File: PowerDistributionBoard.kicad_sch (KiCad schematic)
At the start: 0 parts

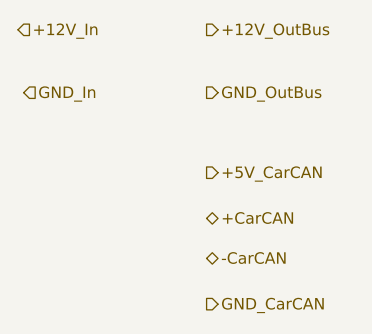
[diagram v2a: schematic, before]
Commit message: add LV pwr dist
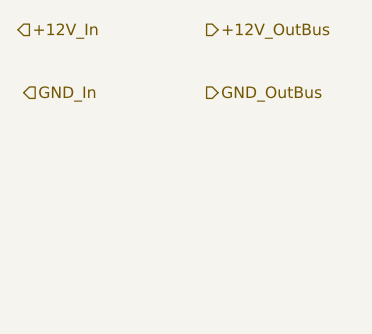
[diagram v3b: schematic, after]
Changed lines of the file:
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@@
-		)
-	)
-	(hierarchical_label "-CarCAN"
-		(shape bidirectional)
-		(at 127.635 104.775 0)
-		(effects
-			(font
-				(size 1.27 1.27)
-			)
-			(justify left)
-		)
-	)
-	(hierarchical_label "+CarCAN"
-		(shape bidirectional)
-		(at 127.635 100.33 0)
-		(effects
-			(font
-				(size 1.27 1.27)
-			)
-			(justify left)
 		)
 	)
@@
 		(effects
 			(font
-				(size 1.27 1.27)
-			)
-			(justify left)
-		)
-	)
-	(hierarchical_label "GND_CarCAN"
-		(shape output)
-		(at 127.635 109.855 0)
-		(effects
-			(font
-				(size 1.27 1.27)
-			)
-			(justify left)
-		)
-	)
-	(hierarchical_label "+5V_CarCAN"
-		(shape output)
-		(at 127.635 95.25 0)
-		(effects
-			(font
